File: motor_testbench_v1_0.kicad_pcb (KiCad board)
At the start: 4 copper layers, 99.5 x 74.5 mm, 256 parts, among them IC1 PJA3402_R1_00001, IC2 VIA2000SD, IC3 MIE1W0505BGLVH-3R-P, IC4 MCP3564RT-E_ST, J1 Conn_01x05_Pin, J10 Conn_01x02_Pin, J11 Conn_01x02_Pin, J12 Conn_01x02_Pin, J13 Conn_01x04_Pin, J2 Conn_01x01_Pin, J3 Conn_01x01_Pin, J4 Conn_01x22_Pin, J7 V_bat_in, J8 V_bat_out, J9 V_bat_secondary, U10 NCV8114BSN330T1G, U11 TPS7A2055PDBVR, U12 TLV75733PDYDR, U13 TPS7A2050PDBVR, U14 TPS7A2033PDBVR, U15 TPS7A2018PDBVRG4, U16 TPS7A2050PDBVR, U18 TPS7A2033PDBVR, U19 TPS7A2045PDBVR, U3 CZ3A05, U4 OPA2328DR, U5 OPA2328DR, U6 MCP1502T-50E/CHY, U7 TPS62933, U8 TPS62933, U9 OPA2387DR

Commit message: Minor Tweaks.
[KiCad Version: 10.0.4]
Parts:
- added C2: 1u, Capacitor_SMD:C_0603_1608Metric_Pad1.08x0.95mm_HandSolder, F.Cu at (165.9, 52.7)
- renumbered C9 to C10, C99 to C100, C100 to C101, C101 to C102, C103 to C104, C104 to C105, C106 to C107, C107 to C108, C108 to C109, C10 to C11, C109 to C110, C110 to C111, C111 to C112, C112 to C113, C113 to C114, C114 to C115, C115 to C116, C116 to C117, C117 to C118, C118 to C119, C11 to C12, C119 to C120, C120 to C121, C121 to C122, C12 to C13, C13 to C14, C14 to C15, C15 to C16, C16 to C17, C17 to C18, C18 to C19, C19 to C20, C20 to C21, C21 to C22, C22 to C23, C23 to C24, C24 to C25, C25 to C26, C26 to C27, C27 to C28, C28 to C29, C29 to C30, C30 to C31, C31 to C32, C32 to C33, C33 to C34, C34 to C35, C35 to C36, C36 to C37, C37 to C38, C38 to C39, C39 to C40, C40 to C41, C41 to C42, C42 to C43, C43 to C44, C44 to C45, C45 to C46, C46 to C47, C47 to C48, C48 to C49, C49 to C50, C50 to C51, C51 to C52, C52 to C53, C53 to C54, C54 to C55, C55 to C56, C56 to C57, C57 to C58, C58 to C59, C59 to C60, C60 to C61, C61 to C62, C62 to C63, C63 to C64, C64 to C65, C65 to C66, C66 to C67, C67 to C68, C68 to C69, C69 to C70, C70 to C71, C71 to C72, C72 to C73, C73 to C74, C74 to C75, C75 to C76, C76 to C77, C77 to C78, C78 to C79, C7 to C8, C79 to C80, C80 to C81, C81 to C82, C82 to C83, C83 to C84, C84 to C85, C85 to C86, C86 to C87, C87 to C88, C88 to C89, C8 to C9, C89 to C90, C90 to C91, C91 to C92, C92 to C93, C93 to C94, C94 to C95, C95 to C96, C96 to C97, C97 to C98
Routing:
- net +3V3_ESP: track 29.2 -> 31.9 mm
- net GND: track 162.6 -> 163.8 mm

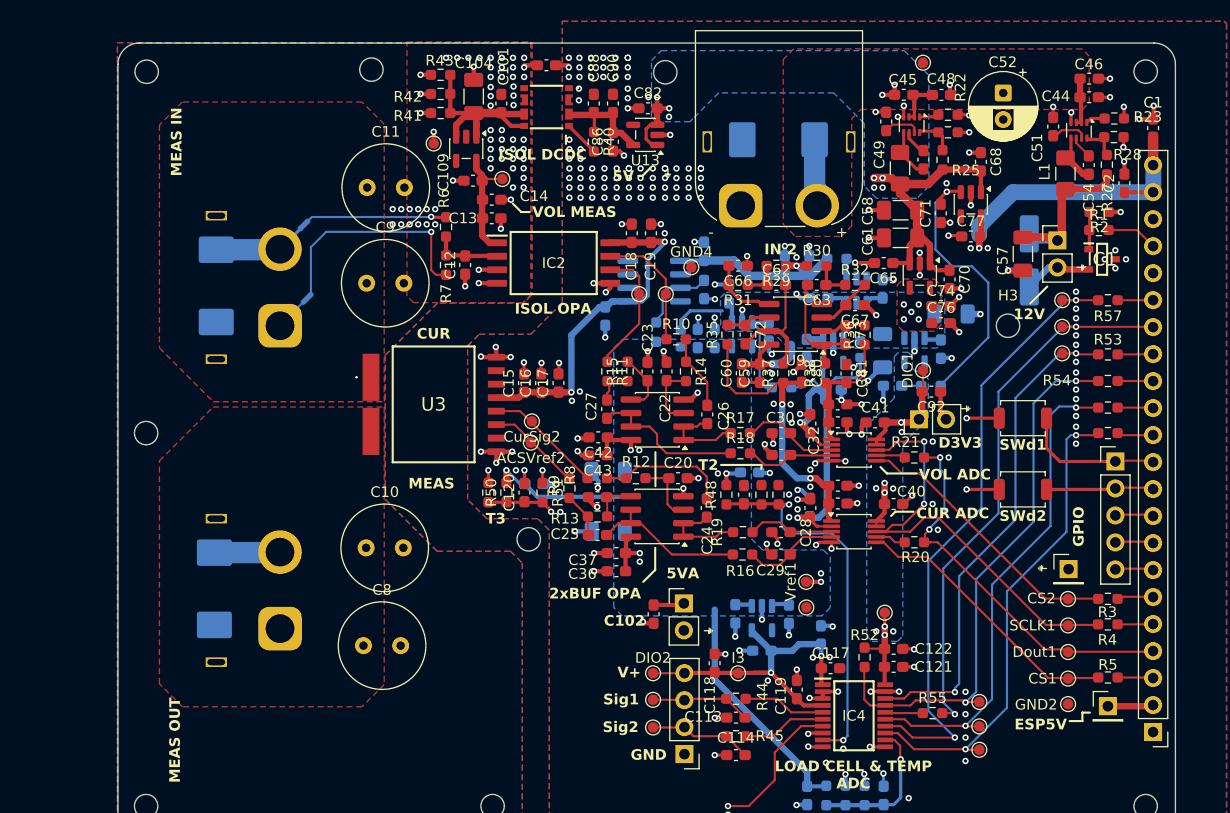
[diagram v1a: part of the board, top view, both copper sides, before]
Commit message: Add Secondary battery voltage measurement. Minor tweaks.
[KiCad Version: 10.0.4]
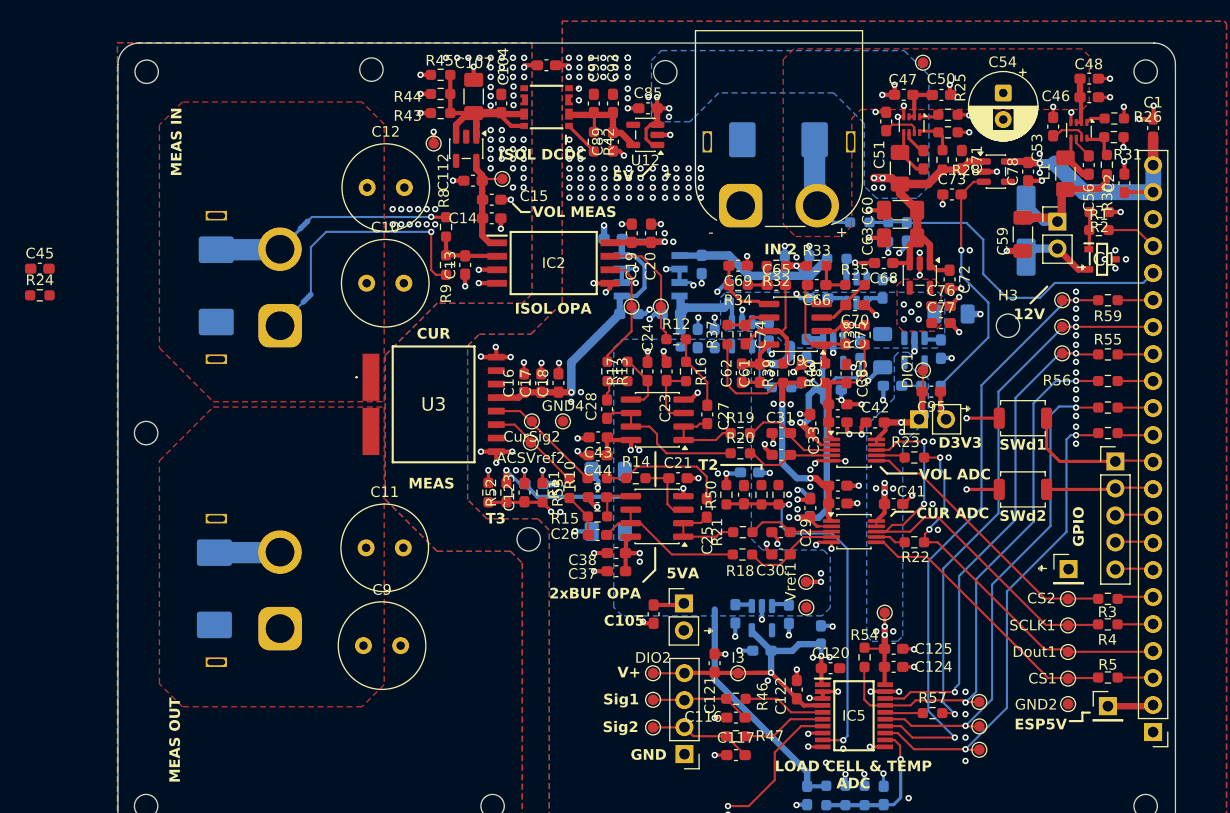
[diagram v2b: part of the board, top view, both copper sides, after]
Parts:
- removed the C69 at (126.4, 62.7)
- removed the R33 at (121.9, 66.7)
- removed the U10 at (121.7, 61.9)
- added C3: 10u, Capacitor_SMD:C_0603_1608Metric_Pad1.08x0.95mm_HandSolder, B.Cu at (145.5, 57.3)
- added C45: 1u, Capacitor_SMD:C_0603_1608Metric_Pad1.08x0.95mm_HandSolder, F.Cu at (63.9, 60.7)
- added C67: 1u, Capacitor_SMD:C_0603_1608Metric_Pad1.08x0.95mm_HandSolder, B.Cu at (123.3, 65.0)
- added C84: 10u, Capacitor_SMD:C_0603_1608Metric_Pad1.08x0.95mm_HandSolder, B.Cu at (117.8, 57.9)
- added IC3: NCV8184DR2G, SamacSys_Parts:SOIC127P600X175-8N, B.Cu at (121.4, 61.4)
- added R24: 10k, Resistor_SMD:R_0603_1608Metric_Pad0.98x0.95mm_HandSolder, F.Cu at (63.9, 63.2)
- added R6: 100k, Resistor_SMD:R_0603_1608Metric_Pad0.98x0.95mm_HandSolder, B.Cu at (141.1, 56.4)
- added R7: 10k, Resistor_SMD:R_0603_1608Metric_Pad0.98x0.95mm_HandSolder, B.Cu at (143.7, 57.3)
- moved GND4 18.9 mm to (113.1, 75.1)
- moved C78 8.14 mm to (156.9, 51.6), turned to 90 degrees
- moved U11 3.87 mm to (153.9, 51.6), turned to 0 degrees
- moved D6 2.82 mm to (156.7, 57.1)
- moved C82 2.23 mm to (119.3, 65.0), turned to 180 degrees
- moved C73 2.06 mm to (149.7, 53.8), turned to 0 degrees
- moved C59 1.85 mm to (156.4, 57.5)
- moved C71 1.81 mm to (150.7, 50.5)
- moved J10 1.78 mm to (159.7, 56.3)
- moved Vsig2 1.38 mm to (119.6, 64.3)
- moved Vsig1 1.27 mm to (122.3, 64.3)
- moved C64 1.26 mm to (126.2, 60.3), turned to 90 degrees
- renumbered C9 to C10, C97 to C100, C98 to C101, C100 to C103, C101 to C104, C102 to C105, C104 to C107, C105 to C108, C10 to C11, C107 to C110, C108 to C111, C109 to C112, C110 to C113, C111 to C114, C112 to C115, C113 to C116, C114 to C117, C115 to C118, C116 to C119, C11 to C12, C117 to C120, C118 to C121, C119 to C122, C120 to C123, C121 to C124, C122 to C125, C12 to C13, C13 to C14, C14 to C15, C15 to C16, C16 to C17, C17 to C18, C18 to C19, C19 to C20, C20 to C21, C21 to C22, C22 to C23, C23 to C24, C24 to C25, C25 to C26, C26 to C27, C27 to C28, C28 to C29, C29 to C30, C30 to C31, C31 to C32, C32 to C33, C33 to C34, C34 to C35, C35 to C36, C36 to C37, C37 to C38, C38 to C39, C39 to C40, C40 to C41, C41 to C42, C42 to C43, C43 to C44, C44 to C46, C45 to C47, C46 to C48, C47 to C49, C48 to C50, C49 to C51, C50 to C52, C51 to C53, C52 to C54, C53 to C55, C54 to C56, C55 to C57, C56 to C58, C57 to C59, C58 to C60, C59 to C61, C60 to C62, C61 to C63, C62 to C65, C63 to C66, C65 to C68, C66 to C69, C67 to C70, C68 to C71, C70 to C72, C71 to C73, C72 to C74, C73 to C75, C74 to C76, C76 to C77, C77 to C78, C78 to C79, C79 to C80, C80 to C81, C75 to C82, C81 to C83, C82 to C85, C83 to C86, C84 to C87, C85 to C88, C86 to C89, C8 to C9, C87 to C90, C88 to C91, C89 to C92, C90 to C93, C91 to C94, C92 to C95, C93 to C96, C94 to C97, C95 to C98, C96 to C99, IC3 to IC4, IC4 to IC5, R8 to R10, R9 to R11, R10 to R12, R11 to R13, R12 to R14, R13 to R15, R14 to R16, R15 to R17, R16 to R18, R17 to R19, R18 to R20, R19 to R21, R20 to R22, R21 to R23, R22 to R25, R23 to R26, R24 to R27, R25 to R28, R26 to R29, R27 to R30, R28 to R31, R29 to R32, R30 to R33, R31 to R34, R32 to R35, R34 to R36, R35 to R37, R36 to R38, R37 to R39, R38 to R40, R39 to R41, R40 to R42, R41 to R43, R42 to R44, R43 to R45, R44 to R46, R45 to R47, R46 to R48, R47 to R49, R48 to R50, R49 to R51, R50 to R52, R51 to R53, R52 to R54, R53 to R55, R54 to R56, R55 to R57, R56 to R58, R57 to R59, R58 to R60, R6 to R8, R7 to R9, U11 to U10, U12 to U11, U13 to U12, U14 to U13, U15 to U14, U16 to U15, U18 to U17, U19 to U18
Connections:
- J4 pad 18: /ESP_GPIO5 -> V_secondary_Bat
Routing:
- net V_secondary_Bat: track 0.00 -> 32.5 mm
- net GND: track 163.8 -> 174.8 mm, vias 273 -> 279
- net +3V3_ESP: track 31.9 -> 23.1 mm
- net Net-(U10-EN): track 7.33 -> 0.00 mm
- net +5V_Ratiometric_Supply: track 31.9 -> 35.8 mm
- net +VBat_Secondary: track 15.5 -> 19.3 mm
- net Net-(U11-EN): track 26.6 -> 23.8 mm
- net +5V5_bus: track 22.6 -> 25.1 mm
- net +6V_Buck_Out: track 35.5 -> 34.1 mm
- net /Voltage and Current Measurements/Vout_ref: track 12.3 -> 11.2 mm
- net +12V_Fan_Supply: track 6.44 -> 7.05 mm

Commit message: Add full ESP32 DevKit Length PCB.
[KiCad Version: 10.0.4]
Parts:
- added H12: MountingHole, MountingHole:MountingHole_2.2mm_M2_DIN965, F.Cu at (155.6, 65.0)
- added H9: MountingHole, MountingHole:MountingHole_2.2mm_M2_DIN965, F.Cu at (158.2, 111.2)
- added U1: ESP32-S3-DevKitC, custom_footprints:ESP32-S3-DevKitC_with_3DModel, F.Cu at (168.7, 51.0)
- C54: footprint Capacitor_THT:CP_Radial_D6.3mm_P2.50mm -> Capacitor_SMD:CP_Elec_6.3x5.3
- D6: footprint Diode_SMD:D_SMA_Handsoldering -> Diode_SMD:D_SMA
- moved H1 27.6 mm to (195.5, 42.1)
- moved H7 27.6 mm to (195.5, 111.2)
- moved J4 26.9 mm to (195.6, 104.3)
- moved H3 26.8 mm to (167.0, 42.1)
- moved C54 1.02 mm to (154.9, 45.1)
- moved C78 0.72 mm to (156.9, 52.3)
- moved U11 0.72 mm to (153.9, 52.3)
- moved C53 0.24 mm to (159.5, 47.4)
- renumbered H9 to H10, H10 to H11
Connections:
- J4 pad 10: /ESP_GPIO3 -> /ESP_GPIO35
- J4 pad 11: /ESP_GPIO8 -> /ESP_GPIO36
- J4 pad 12: DS_ADC_SPI_CS -> /ESP_GPIO37
- J4 pad 13: DS_ADC_SPI_MOSI -> /ESP_GPIO38
- J4 pad 14: DS_ADC_IRQ -> /ESP_GPIO39
- J4 pad 15: DS_ADC_MCLK -> /ESP_GPIO40
- J4 pad 16: DS_ADC_SPI_MISO -> /ESP_GPIO41
- J4 pad 17: DS_ADC_SPI_SCLK -> /ESP_GPIO42
- J4 pad 18: V_secondary_Bat -> /ESP_GPIO2
- J4 pad 19: FAN_PWM -> /ESP_GPIO1
- J4 pad 2: /ESP_5V -> GND
- J4 pad 20: /ESP_EN/RST -> /UART_RX
- J4 pad 21: +3V3_ESP -> /UART_TX
- J4 pad 22: +3V3_ESP -> GND
- J4 pad 3: /ESP_GPIO14 -> /ESP_GPIO19
- J4 pad 4: MISO -> /ESP_GPIO20
- J4 pad 5: /ESP_GPIO12 -> /ESP_GPIO21
- J4 pad 6: /ESP_GPIO11 -> /ESP_GPIO47
- J4 pad 7: /ESP_GPIO10 -> /ESP_GPIO48
- J4 pad 8: /ESP_GPIO9 -> /ESP_GPIO45
- J4 pad 9: /ESP_GPIO46 -> /ESP_GPIO0
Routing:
- net GND: track 174.8 -> 193.1 mm, vias 279 -> 288
- net /UART_TX: track 0.00 -> 4.05 mm
- net /UART_RX: track 0.00 -> 4.05 mm
- net /ESP_GPIO48: track 0.00 -> 4.05 mm
- net /ESP_GPIO47: track 0.00 -> 4.05 mm
- net /ESP_GPIO45: track 0.00 -> 4.05 mm
- net /ESP_GPIO42: track 0.00 -> 4.05 mm
- net /ESP_GPIO41: track 0.00 -> 4.05 mm
- net /ESP_GPIO40: track 0.00 -> 4.05 mm
- net /ESP_GPIO39: track 0.00 -> 4.05 mm
- net /ESP_GPIO38: track 0.00 -> 4.05 mm
- net /ESP_GPIO37: track 0.00 -> 4.05 mm
- net /ESP_GPIO36: track 0.00 -> 4.05 mm
- net /ESP_GPIO35: track 0.00 -> 4.05 mm
- net /ESP_GPIO21: track 0.00 -> 4.05 mm
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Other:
- board size 99.5 x 74.5 mm -> 126.9 x 74.5 mm

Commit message: Initial switch to ESP32 Module
[KiCad Version: 10.0.4]
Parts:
- added C73: 1u, Capacitor_SMD:C_0603_1608Metric_Pad1.08x0.95mm_HandSolder, B.Cu at (152.1, 52.8)
- C74: renamed from C73; moved to B.Cu
- C79: renamed from C78; moved to B.Cu
- U11: moved to B.Cu
- moved C74 8.19 mm to (154.9, 47.4), turned to -90 degrees
- moved C79 1.85 mm to (158.0, 50.9), turned to -90 degrees
- moved U11 1.85 mm to (155.0, 50.9)
- renumbered C99 to C100, C100 to C101, C101 to C102, C103 to C104, C104 to C105, C105 to C106, C107 to C108, C108 to C109, C110 to C111, C111 to C112, C112 to C113, C113 to C114, C114 to C115, C115 to C116, C116 to C117, C117 to C118, C118 to C119, C119 to C120, C120 to C121, C121 to C122, C122 to C123, C123 to C124, C124 to C125, C125 to C126, C71 to C70, C70 to C71, C74 to C75, C75 to C76, C76 to C77, C77 to C78, C79 to C80, C80 to C81, C81 to C82, C82 to C83, C83 to C84, C84 to C85, C85 to C86, C86 to C87, C87 to C88, C88 to C89, C89 to C90, C90 to C91, C91 to C92, C92 to C93, C93 to C94, C94 to C95, C95 to C96, C96 to C97, C97 to C98, C98 to C99, J4 to J1, J1 to J2, J2 to J3, J3 to J4, R6 to R3, R7 to R4, R3 to R5, R4 to R6, R5 to R7
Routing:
- net Net-(U11-EN): track 23.5 -> 31.1 mm, vias 1 -> 2
- net GND: track 193.1 -> 196.4 mm, vias 288 -> 292
- net +6V_Buck_Out: track 33.8 -> 36.4 mm, vias 4 -> 6
- net +3V3_ESP: track 22.8 -> 21.6 mm, vias 1 -> 0
